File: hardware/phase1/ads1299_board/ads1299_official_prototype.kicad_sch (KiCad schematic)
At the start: 165 parts, among them J1 Conn_02x05_Odd_Even, J3 Conn_02x10_Odd_Even, J6 36PIN_IDC, U1 ADS1299IPAG, U10 24AA256-I/ST, U2 REG104GA-5, U3 TPS70302PWP, U4 OPA376, U5 TPS60403DBVT, U6 TPS73225DBVT, U7 TPS72325DBVT

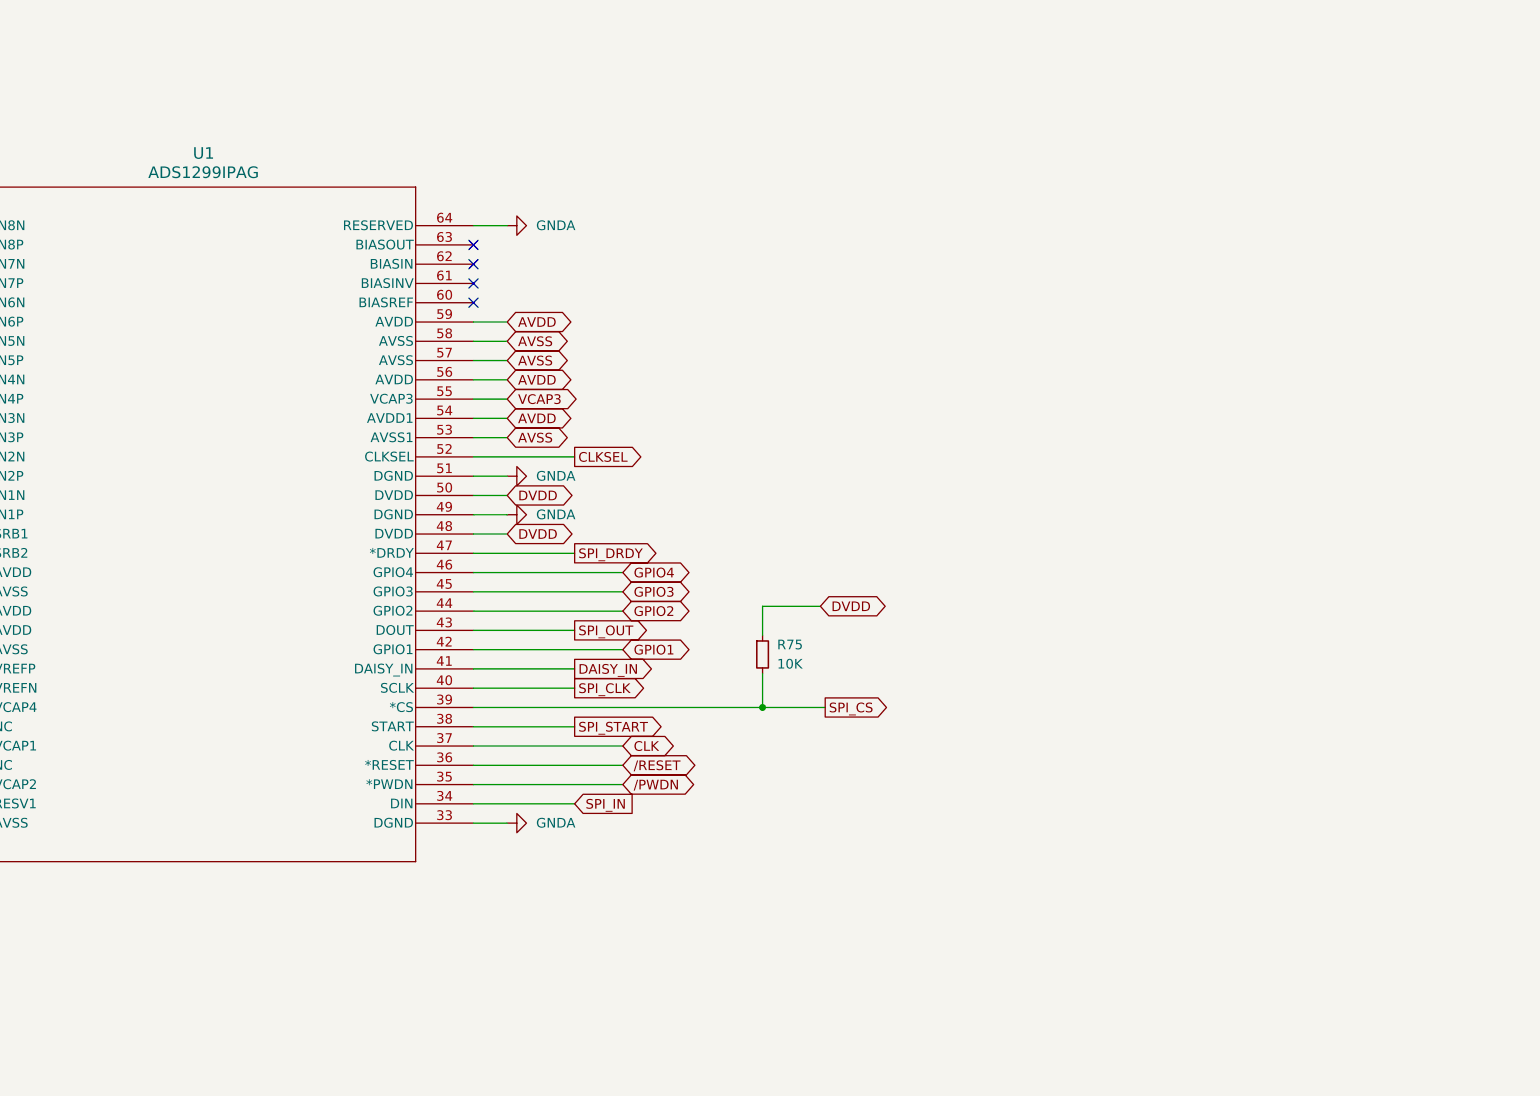
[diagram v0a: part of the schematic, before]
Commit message: ADS1299 Updated J3 and organized routes, speeding up placement and routing
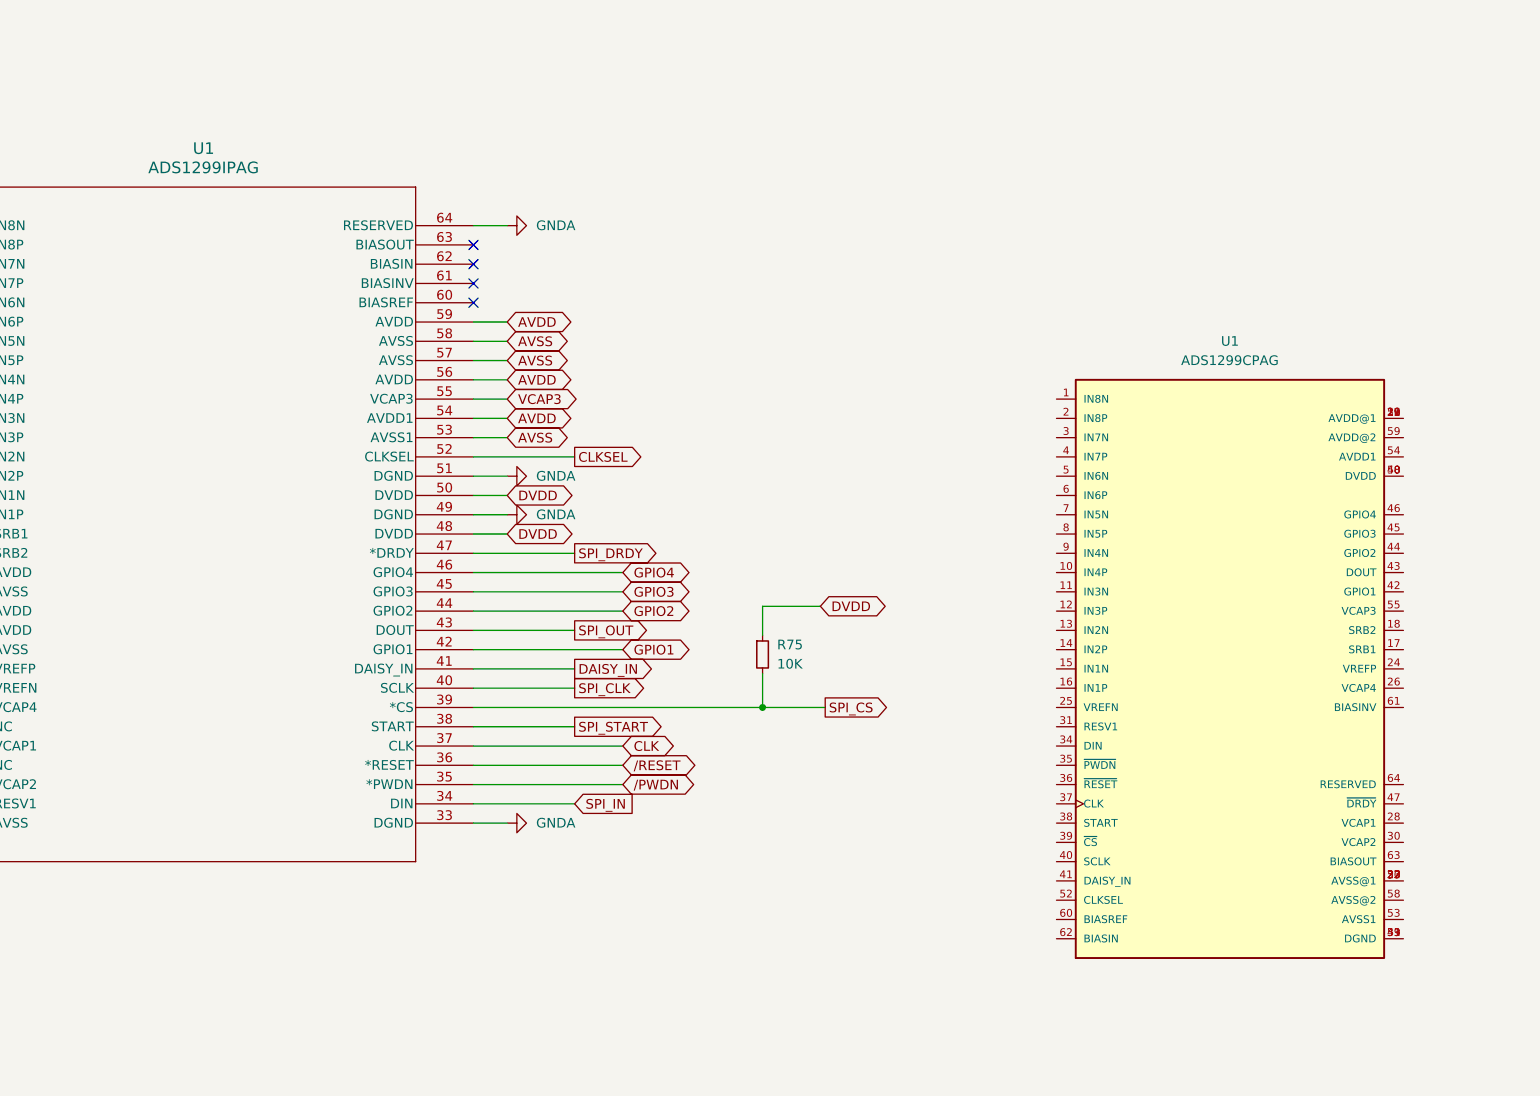
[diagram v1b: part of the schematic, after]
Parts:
- added U1: ADS1299CPAG, ADS1299CPAG:QFP64P50_1200X1200X120L60X22N, symbol ADS1299CPAG:ADS1299CPAG
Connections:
- new net: U1.19 (AVDD@1), U1.21 (AVDD@1), U1.22 (AVDD@1), U1.56 (AVDD@1)
- new net: U1.20 (AVSS@1), U1.23 (AVSS@1), U1.32 (AVSS@1), U1.57 (AVSS@1)
- new net: U1.33 (DGND), U1.49 (DGND), U1.51 (DGND)
- new net: U1.48 (DVDD), U1.50 (DVDD)

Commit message: Schematic changes, no more power stuff from external board. Layout work, added power stuff, lots to do
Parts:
- removed 10_C1, 10_C3: 0.1uF, GRM188R71H104KA93D:CAPC1608X90N, symbol Device:C_Small
- removed 10_C2: 0.01uF, GRM188R71H103KA01D:CAPC1608X90N, symbol Device:C_Small
- removed 10_C25: 10uF, symbol Device:C_Small
- removed 10_C30, 10_C38, 10_C40, 10_C41: 68uF, symbol Device:C_Polarized_Small
- removed 10_C31: 2.2uF, symbol Device:C_Small
- removed 10_C4: 10uF, GRM219R61A106KE44D:CAPC2012X95N, symbol Device:C_Small
- removed 10_C9: 0.01uF, symbol Device:C_Small
- removed 10_J12: TSW-102-07-T-S, TSW-102-07-T-S:SAMTEC_TSW-102-07-T-S, symbol TSW-102-07-T-S:TSW-102-07-T-S
- removed 10_J13A, 10_J13B: Conn_01x02, symbol Connector_Generic:Conn_01x02
- removed 10_J14: Screw_Terminal_01x06, symbol Connector:Screw_Terminal_01x06
- removed 10_J2: PJ-102B, PJ_102B:CUI_PJ-102B, symbol PJ-102B:PJ-102B
- removed 10_J9: AMPPWR, symbol Connector_Generic:Conn_02x03_Odd_Even
- removed 10_R14: 9.31K, RC0603FR-079K31L:RC0603N_YAG, symbol Device:R_Small
- removed 10_R15: 51.1K, RC0603FR_0751K1L:RC0603N_YAG, symbol Device:R_Small
- removed 10_R16, 10_R17: 30.1K, RC0603FR-0730K1L:RC0603N_YAG, symbol Device:R_Small
- removed 10_R2: 10K, RC0603FR-0710KL:RESC1607X60N, symbol Device:R_Small
- removed 10_S3: RESET, symbol Switch:SW_Push
- removed 10_U7: TPS79618DCQ, TPS79618DCQ:SOT127P706X180-6N, symbol PH_TPS79618DCQ:TS5205CX525_RFG
- removed J1: Conn_02x05_Odd_Even, symbol Connector_Generic:Conn_02x05_Odd_Even
- removed L3: 3.3uH, MLZ2012A3R3W:INDC2012X87N, symbol MLZ2012A3R3W:MLZ2012A3R3W
- removed U1: ADS1299CPAG, ADS1299CPAG:QFP64P50_1200X1200X120L60X22N, symbol ADS1299CPAG:ADS1299CPAG
- removed U2: REG104GA-5, REG104GA-5:SOT127P706X180-6N, symbol REG104GA-5:REG104GA-5
- removed U3: TPS70302PWP, TPS70302PWP:SOP65P640X120-25N, symbol TPS70302PWP:TPS70302PWP
- added J2, J9: 1725656, 1725656:PHOENIX_1725656, symbol 1725656:1725656
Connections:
- net GND: now also U5.4 (GND), J9.2
- new net +2V5: J2.1
- new net +3.3V: J9.1
- new net -2V5: J2.2
- no-connect marks 12 -> 23
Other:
- moved on the sheet: AIN1, C1, C10, C11, C12, C13, C14, C15, C16, C17, C18, C19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
